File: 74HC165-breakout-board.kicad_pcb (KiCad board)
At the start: 2 copper layers, 88 x 40 mm, 34 parts, among them J1 Conn_01x05, J10 Conn_01x04, J2 Conn_01x05, J3 Conn_01x05, J4 Conn_01x05, J5 Conn_01x05, J6 Conn_01x05, J7 Conn_01x05, J8 Conn_01x05, J9 Conn_01x05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

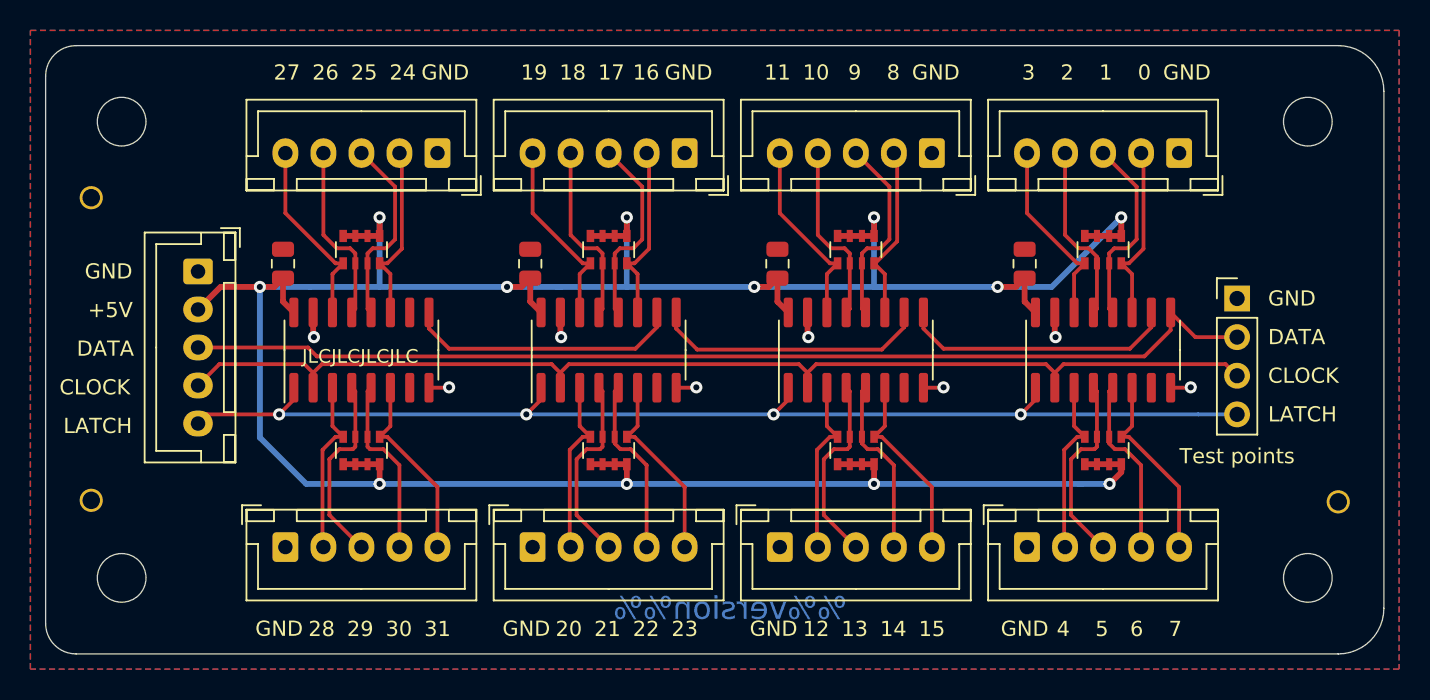
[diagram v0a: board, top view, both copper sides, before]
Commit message: Add via stitching Fixes #4
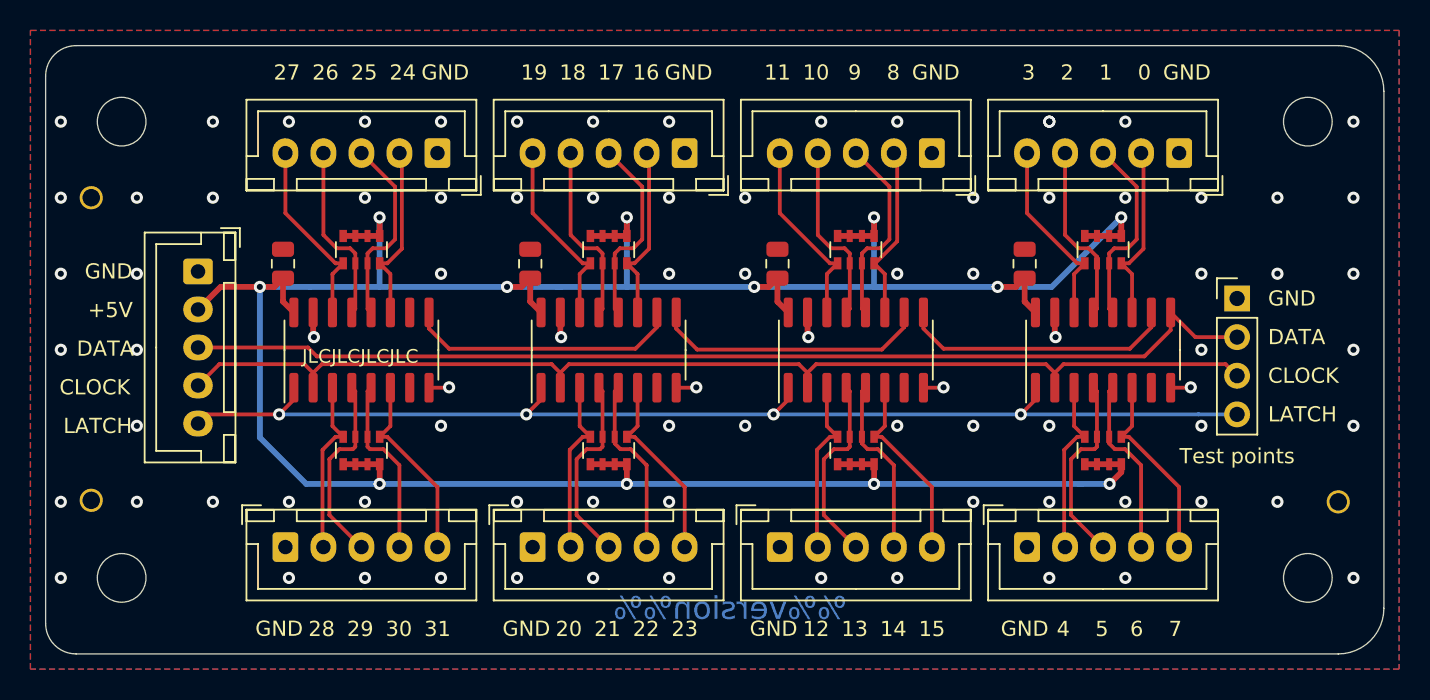
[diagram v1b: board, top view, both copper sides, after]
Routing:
- net GND: vias 8 -> 85
